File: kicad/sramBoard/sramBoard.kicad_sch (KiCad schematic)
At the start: 1 part, among them J1 Conn_02x20_Top_Bottom

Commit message: cdcdcdcdcdcdcdcdcdcdc
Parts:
- J1: footprint (none) -> Connector_IDC:IDC-Header_2x20_P2.54mm_Horizontal
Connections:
- net +10V: now also J1.7 (Pin_7), J1.8 (Pin_8), J1.9 (Pin_9); no longer J1.27 (Pin_27), J1.28 (Pin_28)
- net +5V: now also J1.10 (Pin_10), J1.11 (Pin_11), J1.12 (Pin_12), J1.13 (Pin_13), J1.14 (Pin_14); no longer J1.29 (Pin_29), J1.30 (Pin_30), J1.31 (Pin_31), J1.32 (Pin_32)
- net 1_16_5V_DEMUX_NOTOUT/D: now also J1.5 (Pin_5); no longer J1.25 (Pin_25)
- net 1_16_5V_DEMUX_NOTOUT/S_{0}: now also J1.1 (Pin_1); no longer J1.21 (Pin_21)
- net 1_16_5V_DEMUX_NOTOUT/S_{1}: now also J1.2 (Pin_2); no longer J1.22 (Pin_22)
- net 1_16_5V_DEMUX_NOTOUT/S_{2}: now also J1.3 (Pin_3); no longer J1.23 (Pin_23)
- net 1_16_5V_DEMUX_NOTOUT/S_{3}: now also J1.4 (Pin_4); no longer J1.24 (Pin_24)
- net 8BIT_ROW15/BL_{0}_: now also J1.21 (Pin_21); no longer J1.1 (Pin_1)
- net 8BIT_ROW15/BL_{1}_: now also J1.23 (Pin_23); no longer J1.3 (Pin_3)
- net 8BIT_ROW15/BL_{2}_: now also J1.25 (Pin_25); no longer J1.5 (Pin_5)
- net 8BIT_ROW15/BL_{3}_: now also J1.27 (Pin_27); no longer J1.7 (Pin_7)
- net 8BIT_ROW15/BL_{4}_: now also J1.29 (Pin_29); no longer J1.9 (Pin_9)
- net 8BIT_ROW15/BL_{5}_: now also J1.31 (Pin_31); no longer J1.11 (Pin_11)
- net 8BIT_ROW15/BL_{6}_: now also J1.33 (Pin_33); no longer J1.13 (Pin_13)
- net 8BIT_ROW15/BL_{7}_: now also J1.35 (Pin_35); no longer J1.15 (Pin_15)
- net 8BIT_ROW15/~{BL_{0}}_: now also J1.22 (Pin_22); no longer J1.2 (Pin_2)
- net 8BIT_ROW15/~{BL_{1}}_: now also J1.24 (Pin_24); no longer J1.4 (Pin_4)
- net 8BIT_ROW15/~{BL_{2}}_: now also J1.26 (Pin_26); no longer J1.6 (Pin_6)
- net 8BIT_ROW15/~{BL_{3}}_: now also J1.28 (Pin_28); no longer J1.8 (Pin_8)
- net 8BIT_ROW15/~{BL_{4}}_: now also J1.30 (Pin_30); no longer J1.10 (Pin_10)
- net 8BIT_ROW15/~{BL_{5}}_: now also J1.32 (Pin_32); no longer J1.12 (Pin_12)
- net 8BIT_ROW15/~{BL_{6}}_: now also J1.34 (Pin_34); no longer J1.14 (Pin_14)
- net 8BIT_ROW15/~{BL_{7}}_: now also J1.36 (Pin_36); no longer J1.16 (Pin_16)
- net GND: now also J1.15 (Pin_15), J1.16 (Pin_16), J1.17 (Pin_17), J1.18 (Pin_18), J1.19 (Pin_19), J1.20 (Pin_20), J1.6 (Pin_6); no longer J1.33 (Pin_33), J1.34 (Pin_34), J1.35 (Pin_35), J1.36 (Pin_36)

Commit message: finish main pcb
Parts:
- added C1, C10, C11, C12, C13, C2, C3, C4, C5, C6, C7, C8: 100nC, Capacitor_SMD:C_0603_1608Metric, symbol Device:C
- added C18, C9: 100uC_Polarized, Capacitor_SMD:CP_Elec_6.3x7.7, symbol Device:C_Polarized
- J1: now not fitted; now left out of the parts list
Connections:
- net +10V: now also C10.1, C11.1, C12.1, C13.1, C18.1
- net +5V: now also C1.1, C2.1, C3.1, C4.1, C5.1, C6.1, C7.1, C8.1, C9.1
- net GND: now also C1.2, C10.2, C11.2, C12.2, C13.2, C18.2, C2.2, C3.2, C4.2, C5.2, C6.2, C7.2, C8.2, C9.2

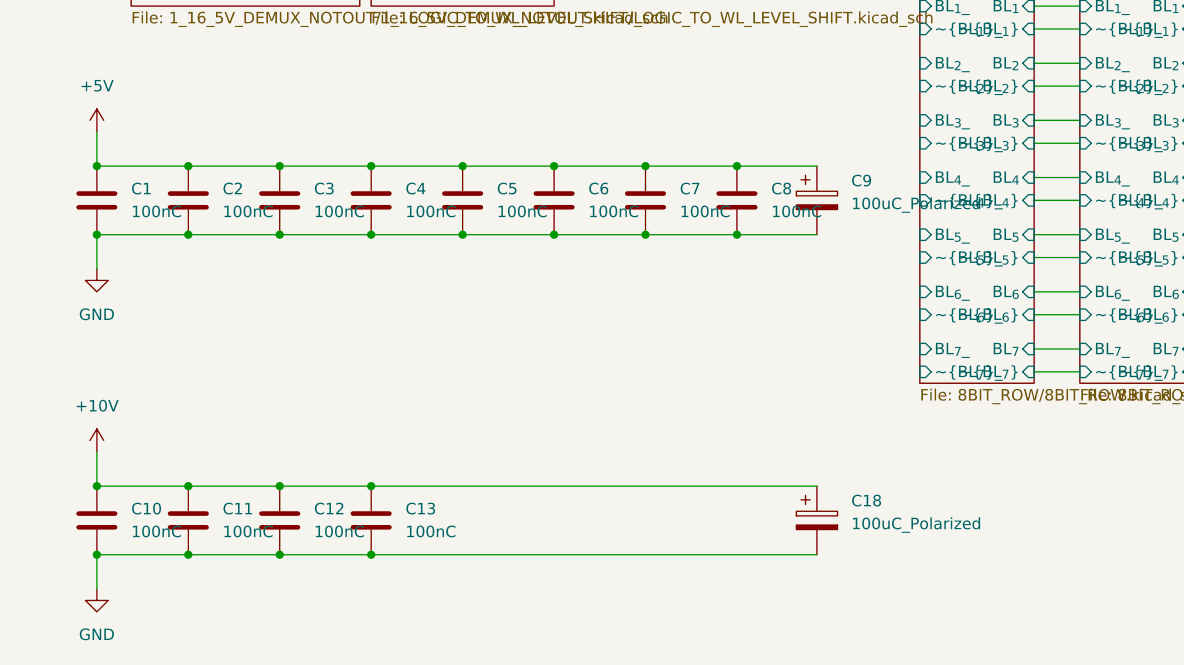
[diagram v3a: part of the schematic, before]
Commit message: fix main ram board
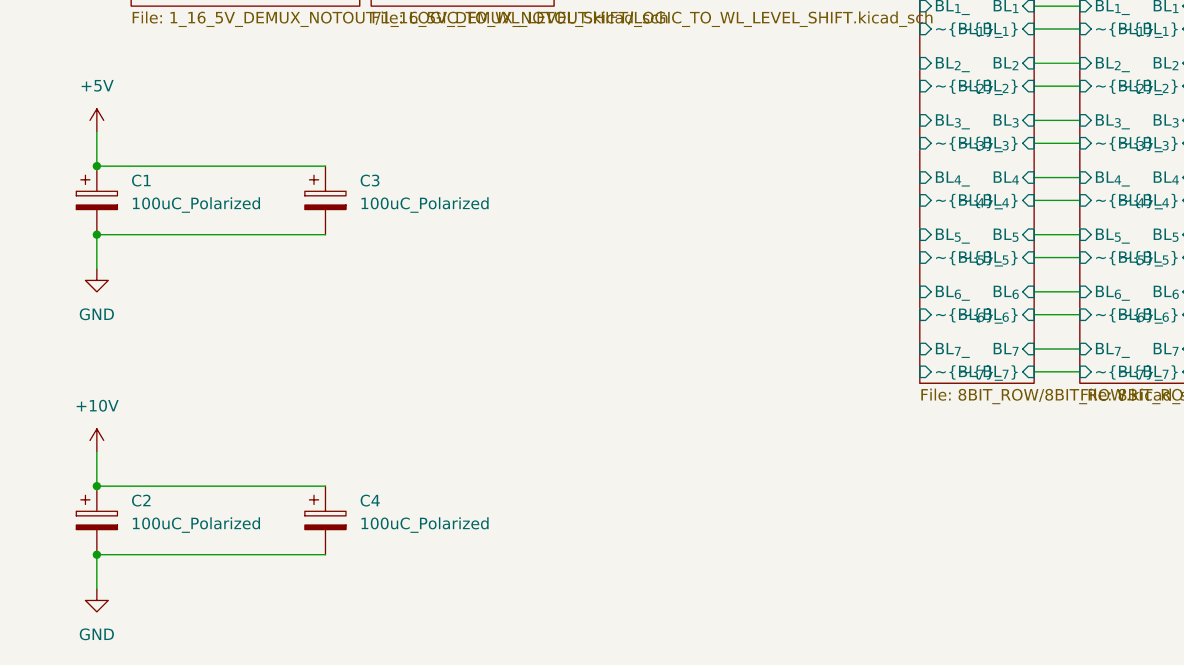
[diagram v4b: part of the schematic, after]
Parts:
- removed C1, C10, C11, C12, C13, C2, C3, C4, C5, C6, C7, C8: 100nC, Capacitor_SMD:C_0603_1608Metric, symbol Device:C
- added C3, C4: 100uC_Polarized, Capacitor_SMD:CP_Elec_6.3x7.7, symbol Device:C_Polarized
- renumbered C9 to C1, C18 to C2
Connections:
- net +10V: now also C4.1
- net +5V: now also C3.1
- net GND: now also C3.2, C4.2
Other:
- moved on the sheet: C1, C2

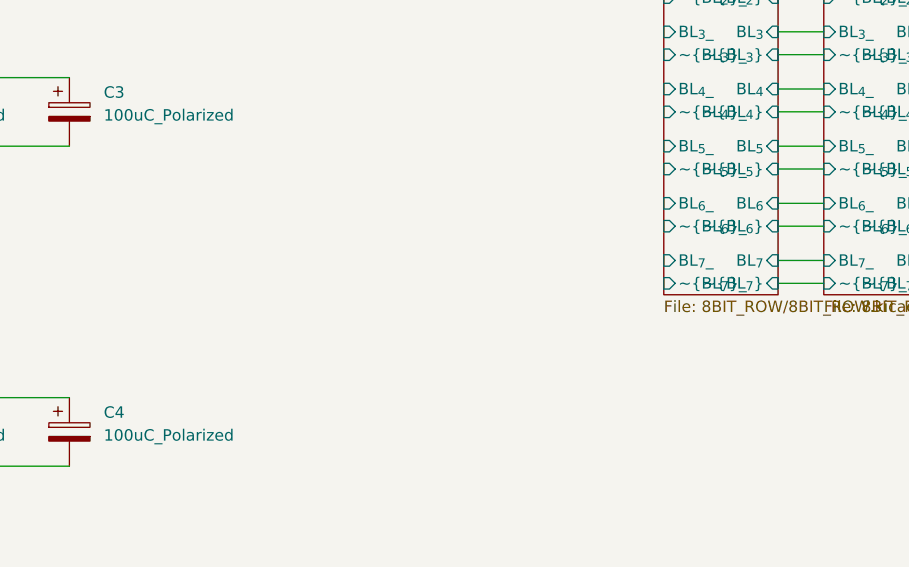
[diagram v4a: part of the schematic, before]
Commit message: add mounting holes
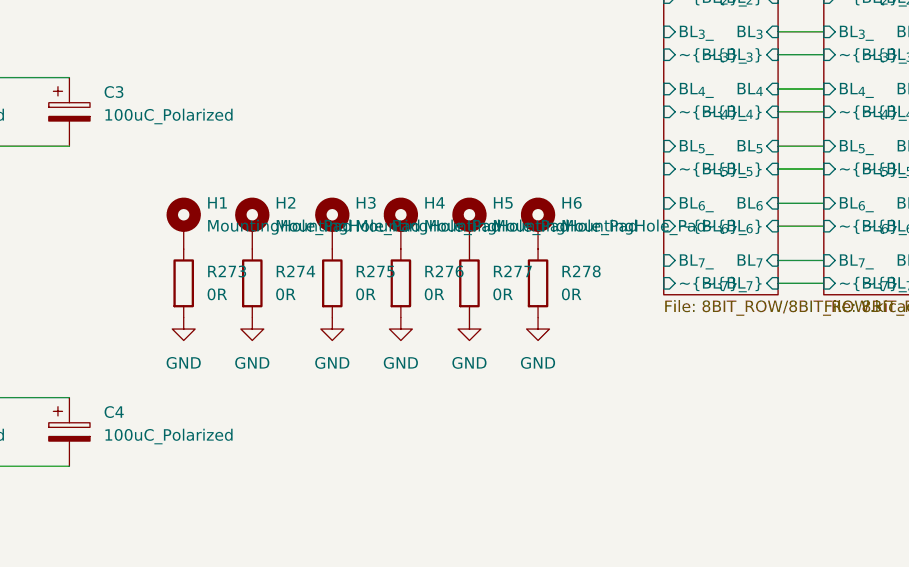
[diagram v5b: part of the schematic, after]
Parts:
- added H1, H2, H3, H4, H5, H6: MountingHole_Pad, MountingHole:MountingHole_3.2mm_M3_DIN965_Pad, symbol Mechanical:MountingHole_Pad
- added R273, R274, R275, R276, R277, R278: 0R, Resistor_SMD:R_1206_3216Metric_Pad1.30x1.75mm_HandSolder, symbol Device:R
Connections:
- net GND: now also R273.2, R274.2, R275.2, R276.2, R277.2, R278.2
- new net: H5.1, R277.1
- new net: H2.1, R274.1
- new net: H3.1, R275.1
- new net: H1.1, R273.1
- new net: H4.1, R276.1
- new net: H6.1, R278.1

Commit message: Add breakout board through holes on main ram board
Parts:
- renumbered R273 to R1, R274 to R2, R275 to R3, R276 to R4, R277 to R5, R278 to R6
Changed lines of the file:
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@@
 		(dnp no)
 		(fields_autoplaced yes)
-		(property "Reference" "#PWR0708"
+		(property "Reference" "#PWR010"
 			(at 76.2 171.45 0)
 			(hide yes)
@@
 			(project "sramBoard"
 				(path "/13380198-0e23-4241-a844-cca11526fb8d"
-					(reference "#PWR0708")
+					(reference "#PWR010")
 					(unit 1)
 				)
@@
 		(dnp no)
 		(fields_autoplaced yes)
-		(property "Reference" "R274"
+		(property "Reference" "R2"
 			(at 69.85 160.0199 0)
 			(show_name no)
@@
 			(project "sramBoard"
 				(path "/13380198-0e23-4241-a844-cca11526fb8d"
-					(reference "R274")
+					(reference "R2")
 					(unit 1)
 				)
@@
 		(dnp no)
 		(fields_autoplaced yes)
-		(property "Reference" "R277"
+		(property "Reference" "R5"
 			(at 93.98 160.0199 0)
 			(show_name no)
@@
 			(project "sramBoard"
 				(path "/13380198-0e23-4241-a844-cca11526fb8d"
-					(reference "R277")
+					(reference "R5")
 					(unit 1)
 				)
@@
 		(dnp no)
 		(fields_autoplaced yes)
-		(property "Reference" "#PWR0710"
+		(property "Reference" "#PWR012"
 			(at 91.44 171.45 0)
 			(hide yes)
@@
 			(project "sramBoard"
 				(path "/13380198-0e23-4241-a844-cca11526fb8d"
-					(reference "#PWR0710")
+					(reference "#PWR012")
 					(unit 1)
 				)
@@
 		(dnp no)
 		(fields_autoplaced yes)
-		(property "Reference" "R275"
+		(property "Reference" "R3"
 			(at 78.74 160.0199 0)
 			(show_name no)
@@
 			(project "sramBoard"
 				(path "/13380198-0e23-4241-a844-cca11526fb8d"
-					(reference "R275")
+					(reference "R3")
 					(unit 1)
 				)
@@
 		(dnp no)
 		(fields_autoplaced yes)
-		(property "Reference" "R273"
+		(property "Reference" "R1"
 			(at 62.23 160.0199 0)
 			(show_name no)
@@
 			(project "sramBoard"
 				(path "/13380198-0e23-4241-a844-cca11526fb8d"
-					(reference "R273")
+					(reference "R1")
 					(unit 1)
 				)
@@
 		(dnp no)
 		(fields_autoplaced yes)
-		(property "Reference" "#PWR0707"
+		(property "Reference" "#PWR09"
 			(at 67.31 171.45 0)
 			(hide yes)
@@
 			(project "sramBoard"
 				(path "/13380198-0e23-4241-a844-cca11526fb8d"
-					(reference "#PWR0707")
+					(reference "#PWR09")
 					(unit 1)
 				)
@@
 		(dnp no)
 		(fields_autoplaced yes)
-		(property "Reference" "R276"
+		(property "Reference" "R4"
 			(at 86.36 160.0199 0)
 			(show_name no)
@@
 			(project "sramBoard"
 				(path "/13380198-0e23-4241-a844-cca11526fb8d"
-					(reference "R276")
+					(reference "R4")
 					(unit 1)
 				)
@@
 		(dnp no)
 		(fields_autoplaced yes)
-		(property "Reference" "#PWR0709"
+		(property "Reference" "#PWR011"
 			(at 83.82 171.45 0)
 			(hide yes)
@@
 			(project "sramBoard"
 				(path "/13380198-0e23-4241-a844-cca11526fb8d"
-					(reference "#PWR0709")
+					(reference "#PWR011")
 					(unit 1)
 				)
@@
 		(dnp no)
 		(fields_autoplaced yes)
-		(property "Reference" "#PWR0706"
+		(property "Reference" "#PWR08"
 			(at 59.69 171.45 0)
 			(hide yes)
@@
 			(project "sramBoard"
 				(path "/13380198-0e23-4241-a844-cca11526fb8d"
-					(reference "#PWR0706")
+					(reference "#PWR08")
 					(unit 1)
 				)
@@
 		(dnp no)
 		(fields_autoplaced yes)
-		(property "Reference" "#PWR0711"
+		(property "Reference" "#PWR013"
 			(at 99.06 171.45 0)
 			(hide yes)
@@
 			(project "sramBoard"
 				(path "/13380198-0e23-4241-a844-cca11526fb8d"
-					(reference "#PWR0711")
+					(reference "#PWR013")
 					(unit 1)
 				)
@@
 		(dnp no)
 		(fields_autoplaced yes)
-		(property "Reference" "R278"
+		(property "Reference" "R6"
 			(at 101.6 160.0199 0)
 			(show_name no)
@@
 			(project "sramBoard"
 				(path "/13380198-0e23-4241-a844-cca11526fb8d"
-					(reference "R278")
-					(unit 1)
-				)
+					(reference "R6")
+					(unit 1)
+				)

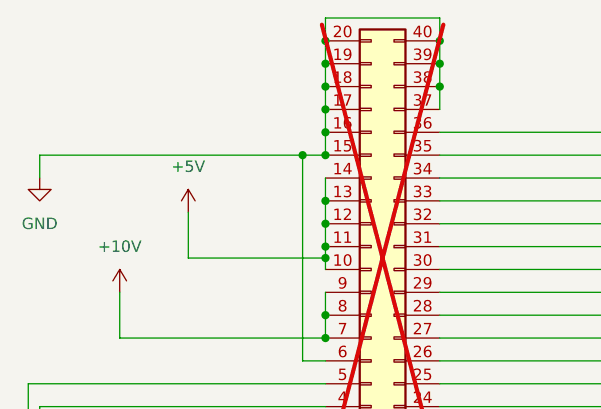
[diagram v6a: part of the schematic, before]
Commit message: update bom, add more capacitors
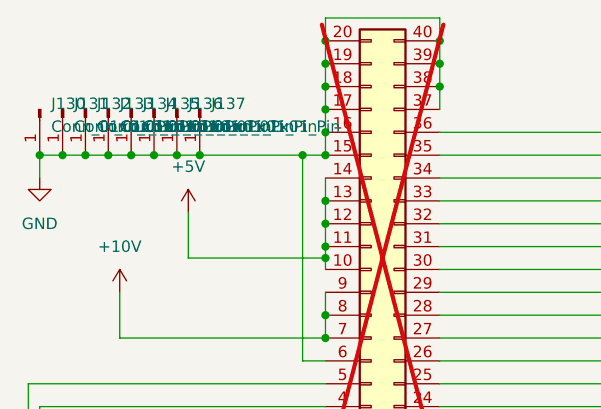
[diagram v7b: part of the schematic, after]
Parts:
- added J130, J131, J132, J133, J134, J135, J136, J137: Conn_01x01_Pin, Connector_Wire:Wire_Pad_18AWG_stranded, symbol Connector:Conn_01x01_Pin
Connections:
- net GND: now also J130.1 (Pin_1), J131.1 (Pin_1), J132.1 (Pin_1), J133.1 (Pin_1), J134.1 (Pin_1), J135.1 (Pin_1), J136.1 (Pin_1), J137.1 (Pin_1)
